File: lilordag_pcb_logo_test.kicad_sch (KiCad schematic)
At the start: 38 parts, among them J1 USB4105-GF-A, Q5 BC846, Q6 BC846, Q7 SSM3J56MFV, Q8 SSM3J56MFV, SW1 PCM12SMTR, SW2 PCM12SMTR, SW3 SW_MEC_5G, U1 ESP32-C3-MINI-1-N4

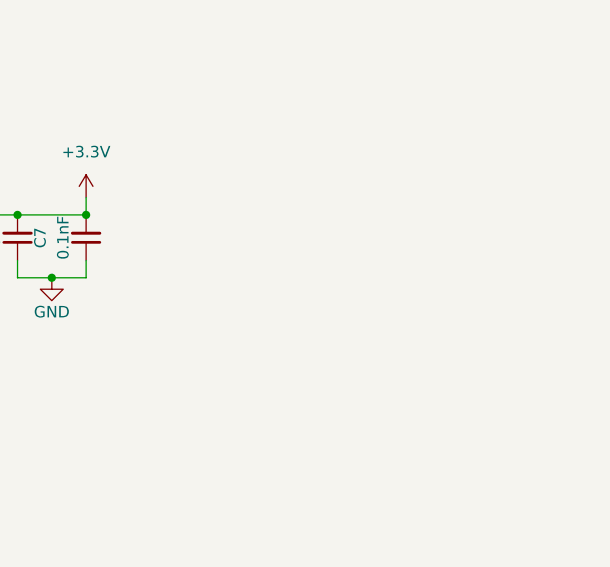
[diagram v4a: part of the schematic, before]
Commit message: Added 4 pin header.
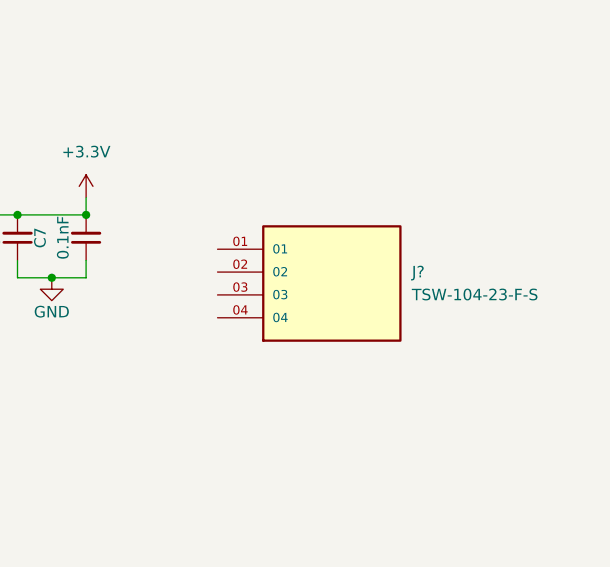
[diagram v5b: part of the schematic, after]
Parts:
- added J?: TSW-104-23-F-S, HEADER-4-PIN:SAMTEC_TSW-104-23-F-S, symbol TSW-104-23-F-S:TSW-104-23-F-S
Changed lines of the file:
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@@
     (pin "1")
+  )
+  (symbol (lib_id "TSW-104-23-F-S:TSW-104-23-F-S") (at 255.27 82.55 0) (unit 1)
+    (in_bom yes) (on_board yes) (fields_autoplaced)
+    (property "Reference" "J?" (id 0) (at 264.16 80.0099 0)
+      (effects (font (size 1.27 1.27)) (justify left))
+    )
+    (property "Value" "TSW-104-23-F-S" (id 1) (at 264.16 82.5499 0)
+      (effects (font (size 1.27 1.27)) (justify left))
+    )
+    (property "Footprint" "HEADER-4-PIN:SAMTEC_TSW-104-23-F-S" (id 2) (at 255.27 82.55 0)
+      (effects (font (size 1.27 1.27)) (justify left bottom) hide)
+    )
+    (property "Datasheet" "" (id 3) (at 255.27 82.55 0)
+      (effects (font (size 1.27 1.27)) (justify left bottom) hide)
+    )
+    (property "PARTREV" "R" (id 4) (at 255.27 82.55 0)
+      (effects (font (size 1.27 1.27)) (justify left bottom) hide)
+    )
+    (property "MANUFACTURER" "Samtec" (id 5) (at 255.27 82.55 0)
+      (effects (font (size 1.27 1.27)) (justify left bottom) hide)
+    )
+    (property "STANDARD" "Manufacturer Recommendations" (id 6) (at 255.27 82.55 0)
+      (effects (font (size 1.27 1.27)) (justify left bottom) hide)
+    )
+    (pin "01")
+    (pin "02")
+    (pin "03")
+    (pin "04")
   )
   (symbol (lib_id "power:+3.3V") (at 59.69 140.335 0) (unit 1)
@@
       (reference "J1") (unit 1) (value "USB4105-GF-A") (footprint "USBC-USB4105-GF-A:GCT_USB4105-GF-A")
     )
+    (path "/d9c20e81-f8af-49a7-81dd-4ff48da1fee4"
+      (reference "J?") (unit 1) (value "TSW-104-23-F-S") (footprint "HEADER-4-PIN:SAMTEC_TSW-104-23-F-S")
+    )
     (path "/ade9b4e0-52ce-45cf-8825-c35ed92dd0f1/d8ebf3b2-57f6-41e6-9126-5e0efd00b212"

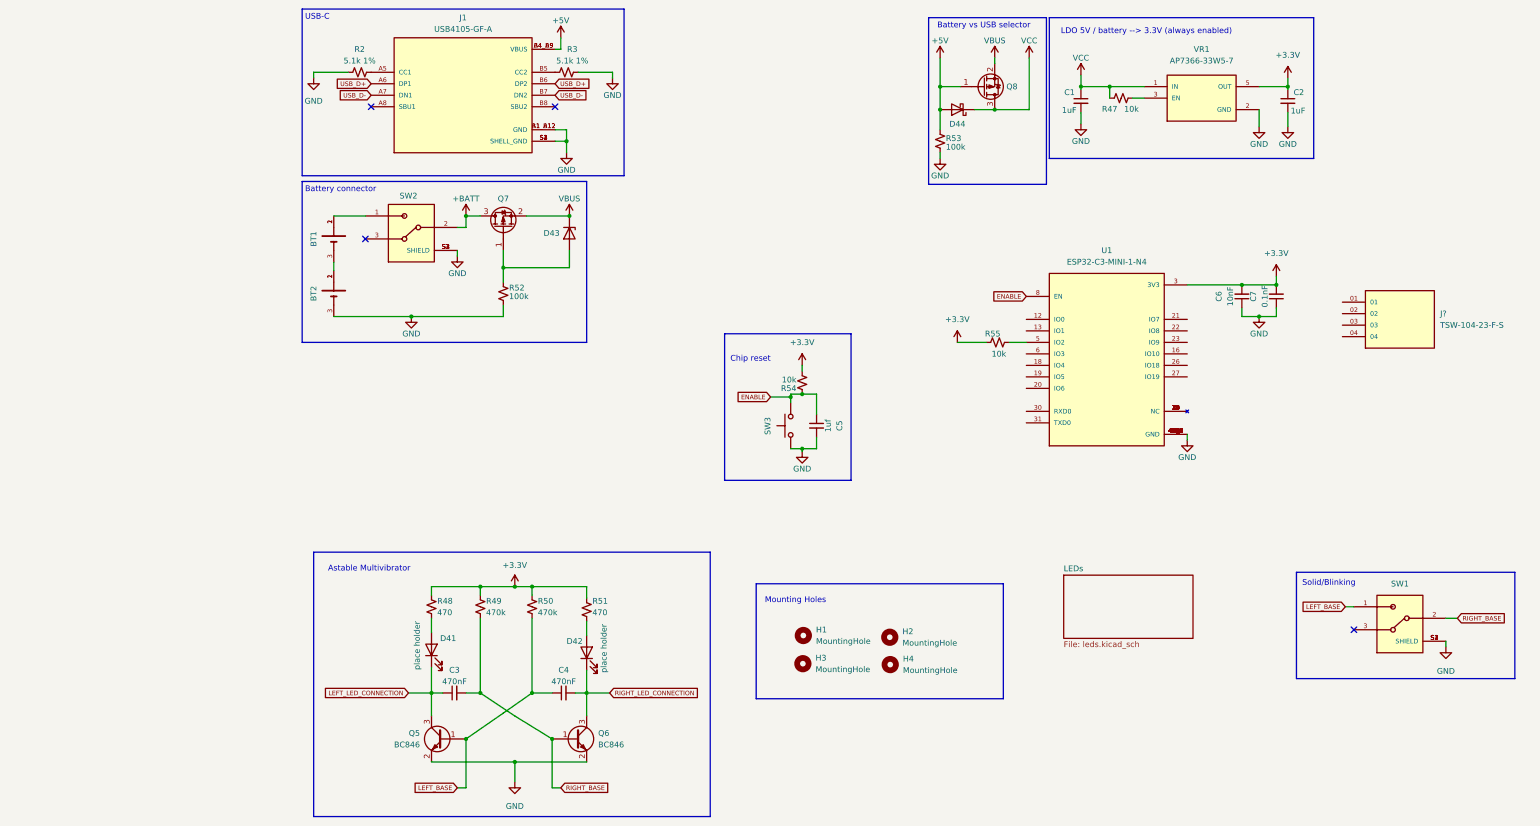
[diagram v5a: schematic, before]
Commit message: Added 6 pin header
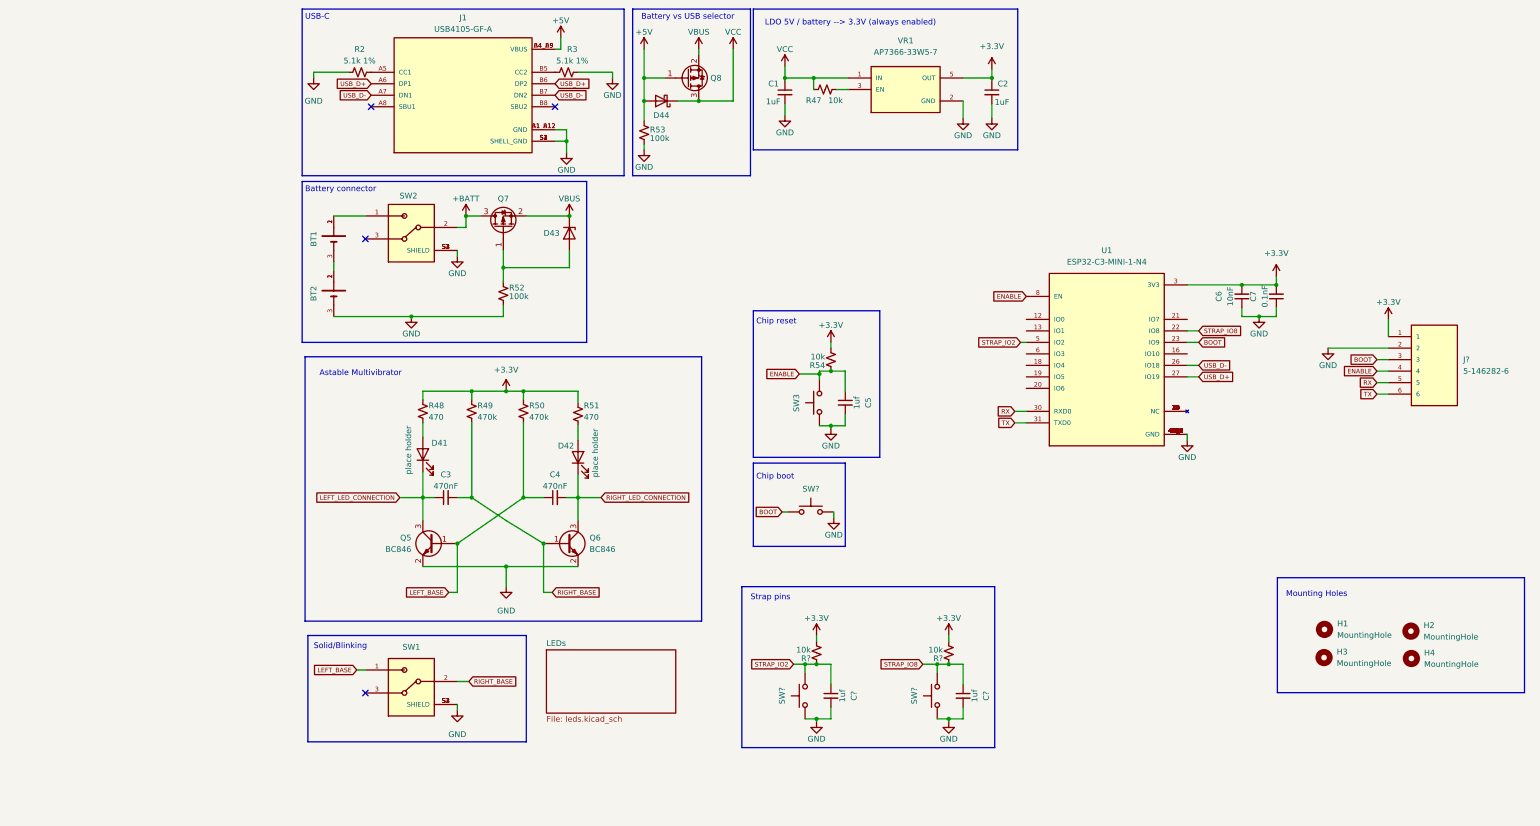
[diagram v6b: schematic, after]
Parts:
- removed J?: TSW-104-23-F-S, HEADER-4-PIN:SAMTEC_TSW-104-23-F-S, symbol TSW-104-23-F-S:TSW-104-23-F-S
- removed R55: 10k, Resistor_SMD:R_0603_1608Metric_Pad0.98x0.95mm_HandSolder, symbol Device:R_Small_US
- added C? (x2): 1uf, Capacitor_SMD:C_0603_1608Metric_Pad1.08x0.95mm_HandSolder, symbol Device:C_Small
- added J?: 5-146282-6, TE_5-146282-6, symbol HEADER-6-PIN:5-146282-6
- added R? (x2): 10k, Resistor_SMD:R_0603_1608Metric_Pad0.98x0.95mm_HandSolder, symbol Device:R_Small_US
- added SW? (x3): SW_MEC_5G, switch-TL3301AF260QG:TL3301AF260QG, symbol Switch:SW_MEC_5G
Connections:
- net +3.3V: now also J?.1, R?.2, R?.2
- net ENABLE: now also J?.4
- net GND: now also C?.2, C?.2, J?.2, SW?.1 (A), SW?.1 (A), SW?.2 (A), SW?.2 (A), SW?.3 (B), SW?.4 (B)
- net USB_D+: now also U1.27 (IO19)
- net USB_D-: now also U1.26 (IO18)
- net STRAP_IO8: now reaches U1.22 (IO8)
- net STRAP_IO8: now also C?.1, R?.1, SW?.3 (B), SW?.4 (B)
- net BOOT: now reaches U1.23 (IO9)
- net BOOT: now also J?.3, SW?.1 (A), SW?.2 (A)
- net RX: now reaches U1.30 (RXD0)
- net RX: now also J?.5
- net TX: now reaches U1.31 (TXD0)
- net TX: now also J?.6
- net STRAP_IO2: now reaches U1.5 (IO2)
- net STRAP_IO2: now also C?.1, R?.1, SW?.3 (B), SW?.4 (B)
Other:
- note added: "Chip boot"
- note added: "Strap pins"
- moved on the sheet: C1, C2, C3, C4, C5, D41, D42, D44, H1, H2, H3, H4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

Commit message: Updated power organization
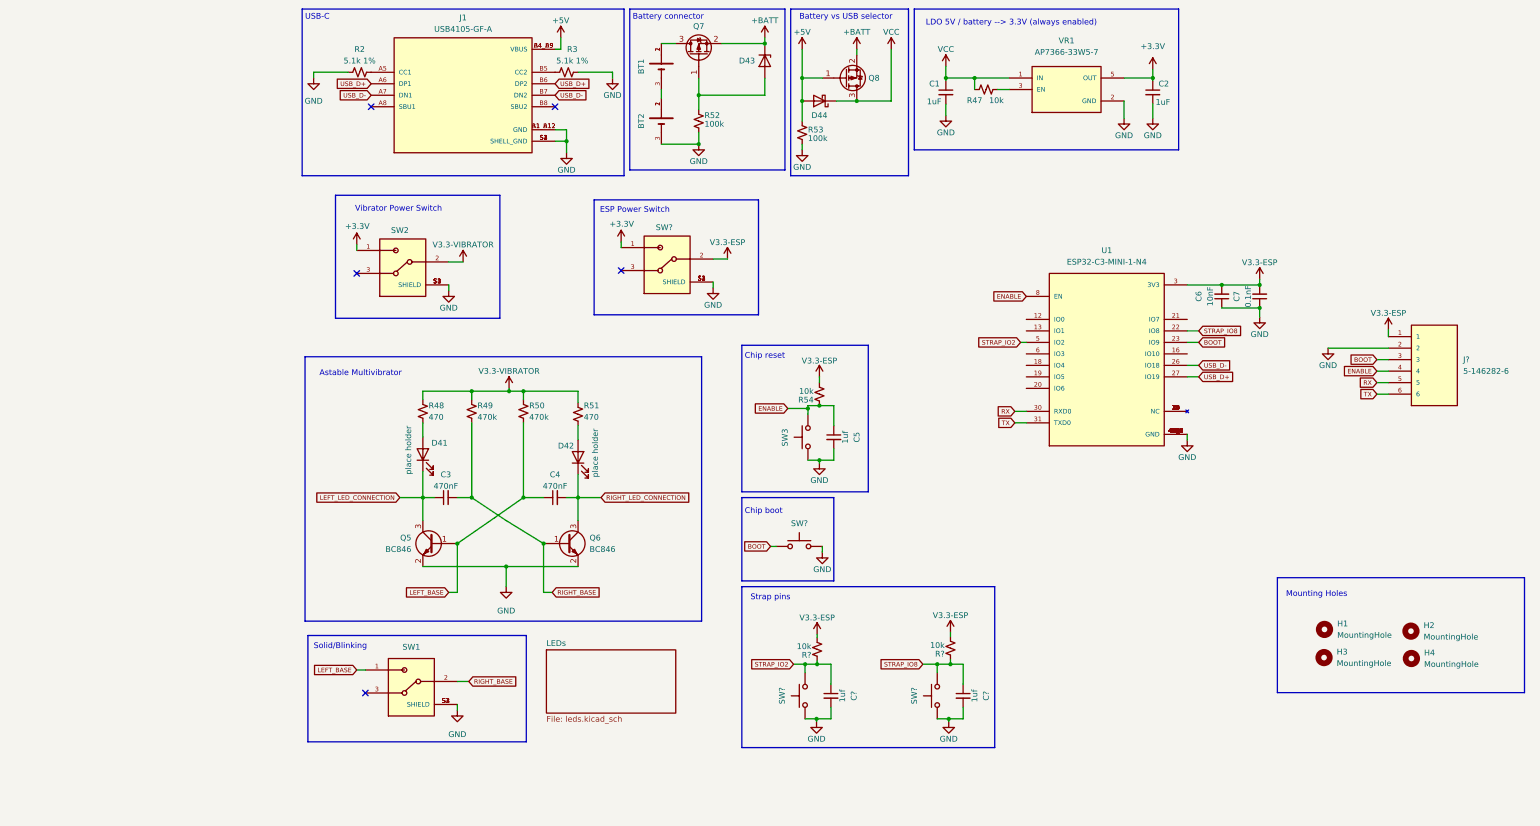
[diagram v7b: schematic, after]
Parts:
- added SW?: PCM12SMTR, PCM12SMTR:SW_PCM12SMTR, symbol PCM12SMTR:PCM12SMTR
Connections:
- net VBUS is gone; now on net +BATT: D43.1 (K), Q7.2 (S), Q8.2 (S)
- net +3.3V: now also SW2.1, SW?.1; no longer C6.2, C7.2, J?.1, R48.1, R49.1, R50.1, R51.1, R54.2, R?.2, R?.2, U1.3 (3V3)
- net +BATT: no longer Q7.3 (D), SW2.2
- net GND: now also SW?.S1 (SHIELD), SW?.S2 (SHIELD), SW?.S3 (SHIELD), SW?.S4 (SHIELD)
- net at BT1.1, BT1.2: now also Q7.3 (D); no longer SW2.1
- new net V3.3-ESP: C6.2, C7.2, J?.1, R54.2, R?.2, R?.2, SW?.2, U1.3 (3V3)
- new net V3.3-VIBRATOR: R48.1, R49.1, R50.1, R51.1, SW2.2
- no-connect marks 4 -> 5
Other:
- note added: "ESP Power Switch"
- note added: "Vibrator Power Switch"
- moved on the sheet: BT1, BT2, C1, C2, C5, C6, C7, D43, D44, Q7, Q8, R47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

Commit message: Fixed most of the power errors
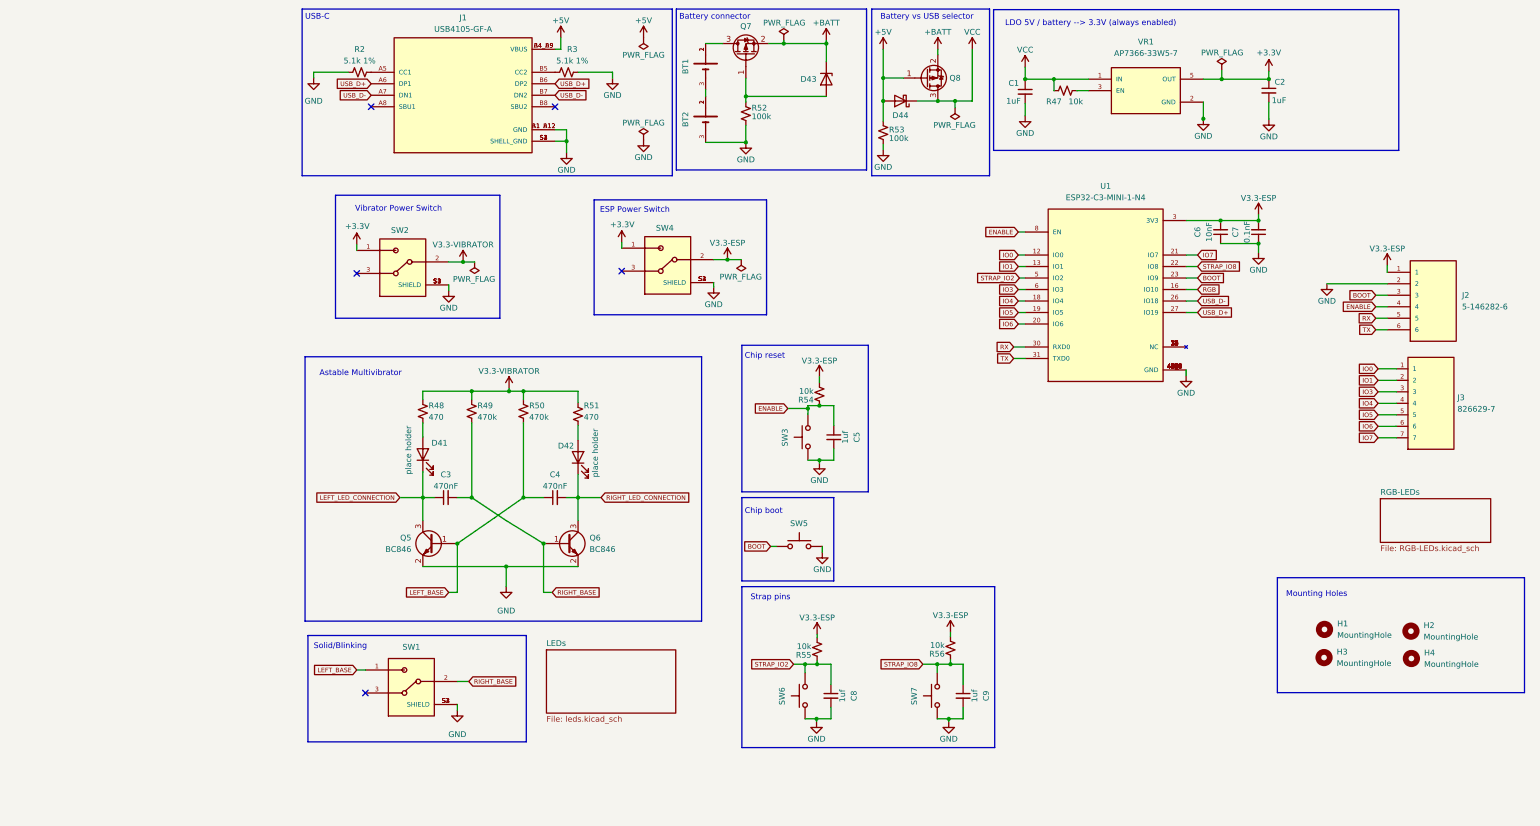
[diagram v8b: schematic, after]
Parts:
- added J3: 826629-7, HEADER-7-PIN:TE_826629-7, symbol 826629-7:826629-7
- BT2: footprint MPD_BK-912-TR -> BK-912-TR-batt-holder:MPD_BK-912-TR
- J2: renamed from J?; footprint TE_5-146282-6 -> HEADER-6-PIN:TE_5-146282-6
- SW3: footprint switch-TL3301AF260QG:TL3301AF260QG -> TL3301AF260QG-button:TL3301AF260QG
- SW5, SW6, SW7: renamed from SW?; footprint switch-TL3301AF260QG:TL3301AF260QG -> TL3301AF260QG-button:TL3301AF260QG
- gave numbers to parts that had none: 5
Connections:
- net IO0: now reaches U1.12 (IO0)
- net IO0: now also J3.1
- net IO1: now reaches U1.13 (IO1)
- net IO1: now also J3.2
- net RGB: now reaches U1.16 (IO10)
- net IO4: now reaches U1.18 (IO4)
- net IO4: now also J3.4
- net IO5: now reaches U1.19 (IO5)
- net IO5: now also J3.5
- net IO6: now reaches U1.20 (IO6)
- net IO6: now also J3.6
- net IO7: now reaches U1.21 (IO7)
- net IO7: now also J3.7
- net IO3: now reaches U1.6 (IO3)
- net IO3: now also J3.3
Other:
- added sheet RGB-LEDs (RGB-LEDs.kicad_sch)
- title: Lilordag logo test -> (none)
- moved on the sheet: BT1, BT2, C1, C2, C6, C7, D43, D44, J2, Q7, Q8, R47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
